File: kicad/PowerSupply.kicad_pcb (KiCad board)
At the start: 2 copper layers, 93 x 116 mm, 111 parts, among them J1 USB_A, J2 Display, J3 USART, J4 Terminal, Q1 MMBT3904, Q2 MMBT3904, Q3 MMBT3904, Q4 MMBT3904, SW1 ENC0 (Voltage), SW2 ENC1 (Current), SW4 RST, U1 OPA4196, U10 STM32F373C8Tx, U2 OPA4196, U3 LD1086D2T33, U5 FQP17P10, U6 FQP17P10, U7 FQP17P10, U8 FQP17P10, Y1 Crystal

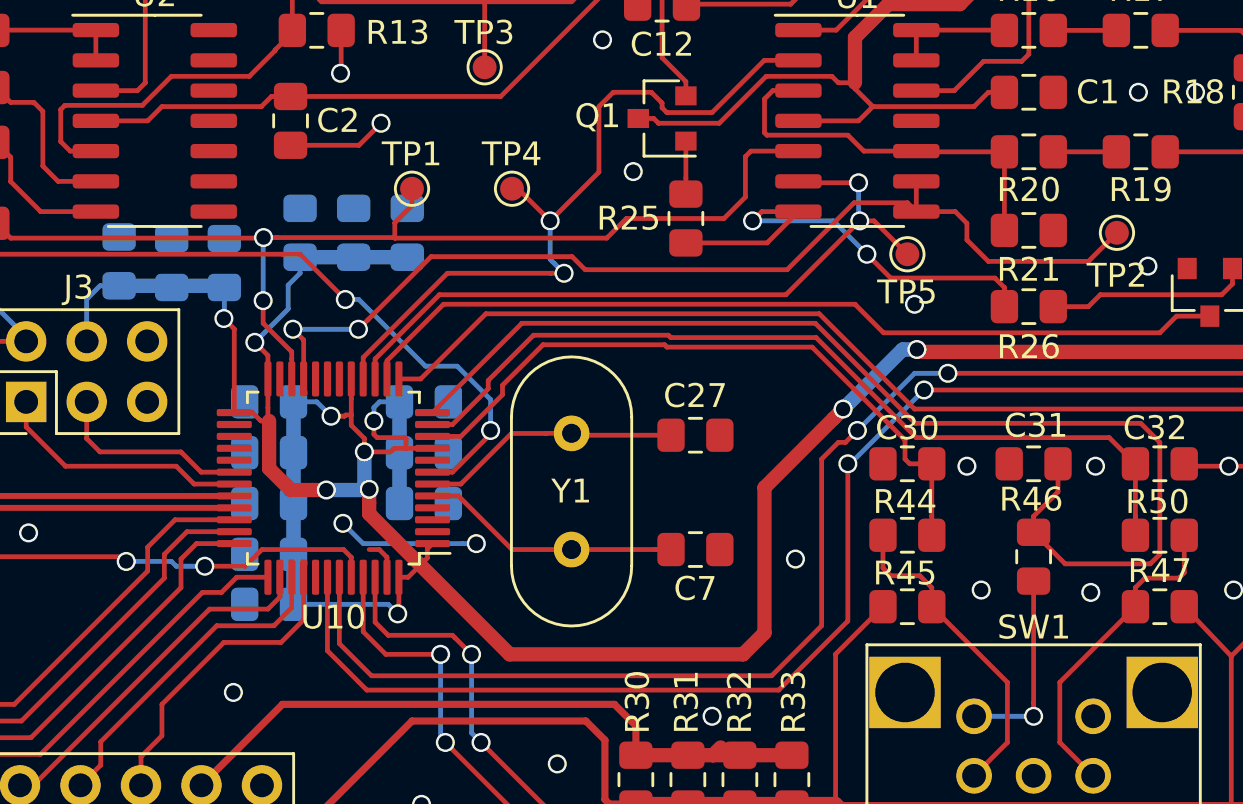
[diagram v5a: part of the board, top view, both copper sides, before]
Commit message: MCU and Crystal caps all grounded at one point
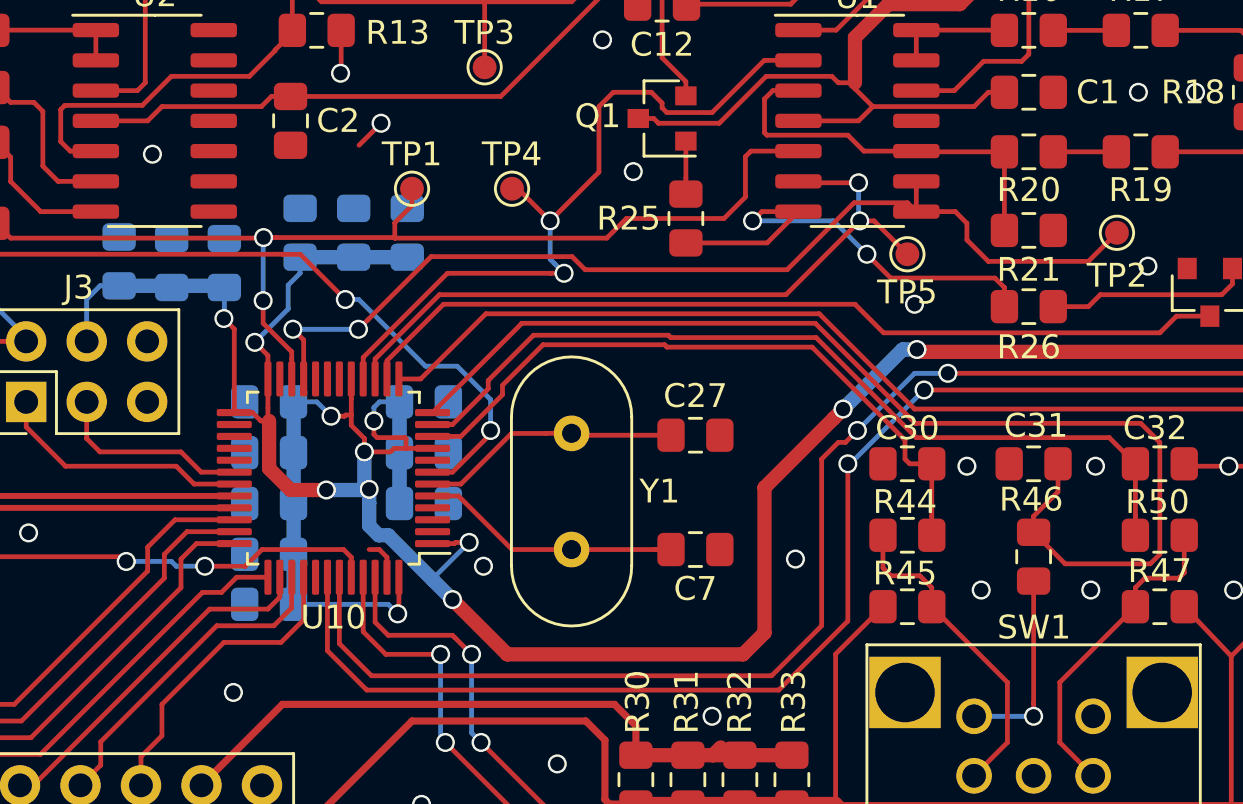
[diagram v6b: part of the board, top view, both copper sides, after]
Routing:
- net GNDREF: track 51.6 -> 42.7 mm, vias 47 -> 48
- net +3V3: track 315.5 -> 317.4 mm, vias 10 -> 12
- net (no net): vias 1 -> 0
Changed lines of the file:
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@@
     (thickness 1.6)
     (drawings 6)
-    (tracks 862)
+    (tracks 864)
     (zones 0)
     (modules 111)
@@
     (descr "Crystal THT HC-49/U http://5hertz.com/pdfs/04404_D.pdf")
     (tags "THT crystalHC-49/U")
-    (fp_text reference Y1 (at 2.44 0 180) (layer F.SilkS)
+    (fp_text reference Y1 (at 2.44 3.7 180) (layer F.SilkS)
       (effects (font (size 1 1) (thickness 0.15)))
     )
@@
   (gr_line (start 0 0) (end 93 0) (layer Edge.Cuts) (width 0.05))
   (gr_line (start 0 0) (end 0 116) (layer Edge.Cuts) (width 0.05))
-  (via (at 5.2 91.7) (size 0.8) (drill 0.6) (layers F.Cu B.Cu) (net 0))
+  (via (at 5.2 91.7) (size 0.8) (drill 0.6) (layers F.Cu B.Cu) (net 1))
   (segment (start 89.525 79.71) (end 89.54 79.725) (width 1) (layer F.Cu) (net 1))
   (segment (start 89.525 76) (end 89.525 79.71) (width 1) (layer F.Cu) (net 1))
@@
   (segment (start 6.025 107) (end 8.525 104.5) (width 0.2) (layer B.Cu) (net 1))
   (segment (start 8.25 88.25) (end 8.25 77.75) (width 0.2) (layer F.Cu) (net 1))
-  (via (at 30.4 101.9) (size 0.8) (drill 0.6) (layers F.Cu B.Cu) (net 1))
-  (segment (start 30.4 101.9) (end 31.251262 102.751262) (width 0.2) (layer B.Cu) (net 1))
-  (segment (start 31.251262 102.751262) (end 35.434325 102.751262) (width 0.2) (layer B.Cu) (net 1))
-  (segment (start 35.434325 102.751262) (end 36.00001 102.751262) (width 0.2) (layer B.Cu) (net 1))
   (via (at 13.8 87.7) (size 0.8) (drill 0.6) (layers F.Cu B.Cu) (net 1))
   (segment (start 13.775 87.725) (end 13.8 87.7) (width 0.2) (layer F.Cu) (net 1))
   (via (at 32 85.1) (size 0.8) (drill 0.6) (layers F.Cu B.Cu) (net 1))
-  (segment (start 28.2 86.025) (end 31.075 86.025) (width 0.2) (layer F.Cu) (net 1))
   (segment (start 31.075 86.025) (end 32 85.1) (width 0.2) (layer F.Cu) (net 1))
   (via (at 30.3 83) (size 0.8) (drill 0.6) (layers F.Cu B.Cu) (net 1))
@@
   (via (at 37.4 78.7) (size 0.8) (drill 0.6) (layers F.Cu B.Cu) (net 1))
   (via (at 54.4 92.7) (size 0.8) (drill 0.6) (layers F.Cu B.Cu) (net 1))
-  (via (at 36.00001 102.751262) (size 0.8) (drill 0.6) (layers F.Cu B.Cu) (net 1))
   (via (at 64.2 91.1) (size 0.8) (drill 0.6) (layers F.Cu B.Cu) (net 1))
   (via (at 87.49 98.3) (size 0.8) (drill 0.6) (layers F.Cu B.Cu) (net 1))
@@
   (via (at 84.1 18.5) (size 0.8) (drill 0.6) (layers F.Cu B.Cu) (net 1))
   (via (at 62 99.5) (size 0.8) (drill 0.6) (layers F.Cu B.Cu) (net 1))
-  (via (at 61.8 104.8) (size 0.8) (drill 0.6) (layers F.Cu B.Cu) (net 1))
+  (via (at 61.8 104.7) (size 0.8) (drill 0.6) (layers F.Cu B.Cu) (net 1))
+  (via (at 22.4 86.4) (size 0.8) (drill 0.6) (layers F.Cu B.Cu) (net 1))
+  (via (at 36.3 103.7) (size 0.8) (drill 0.6) (layers F.Cu B.Cu) (net 1))
   (segment (start 62 3.3) (end 6 3.3) (width 5) (layer F.Cu) (net 2))
   (segment (start 69.3 3.3) (end 62 3.3) (width 5) (layer F.Cu) (net 2))
@@
   (segment (start 75.275 94.7) (end 54.6 94.7) (width 0.6) (layer F.Cu) (net 3))
   (via (at 51.4 97.1) (size 0.8) (drill 0.6) (layers F.Cu B.Cu) (net 3))
-  (segment (start 33.1375 104.1625) (end 33.65 103.65) (width 0.2) (layer F.Cu) (net 3))
-  (segment (start 32.75 104.1625) (end 33.1375 104.1625) (width 0.2) (layer F.Cu) (net 3))
-  (segment (start 33.94179 103.35821) (end 33.65 103.65) (width 0.2) (layer F.Cu) (net 3))
-  (segment (start 34.1625 102.75) (end 33.94179 102.97071) (width 0.2) (layer F.Cu) (net 3))
-  (segment (start 33.94179 102.97071) (end 33.94179 103.35821) (width 0.2) (layer F.Cu) (net 3))
   (via (at 31.3 98.9) (size 0.8) (drill 0.6) (layers F.Cu B.Cu) (net 3))
   (segment (start 31.3 98.9) (end 32.4 98.9) (width 0.2) (layer F.Cu) (net 3))
@@
   (segment (start 32.55 98.75) (end 33.05 98.75) (width 0.2) (layer F.Cu) (net 3))
   (segment (start 33.05 98.75) (end 34.1625 98.75) (width 0.2) (layer F.Cu) (net 3))
-  (segment (start 33.65 103.65) (end 31.50001 101.50001) (width 0.6) (layer F.Cu) (net 3))
   (via (at 31.50001 100.469455) (size 0.8) (drill 0.6) (layers F.Cu B.Cu) (net 3))
   (segment (start 29.7 100.5) (end 31.469465 100.5) (width 0.6) (layer B.Cu) (net 3))
@@
   (segment (start 31.3 100.269445) (end 31.50001 100.469455) (width 0.6) (layer B.Cu) (net 3))
   (segment (start 31.3 98.9) (end 31.3 100.269445) (width 0.6) (layer B.Cu) (net 3))
-  (segment (start 31.50001 101.03514) (end 31.50001 100.469455) (width 0.6) (layer F.Cu) (net 3))
-  (segment (start 31.50001 101.50001) (end 31.50001 101.03514) (width 0.6) (layer F.Cu) (net 3))
   (segment (start 67.7 113.9) (end 81 113.9) (width 0.6) (layer F.Cu) (net 3))
   (segment (start 81 113.9) (end 83.6 111.3) (width 0.6) (layer F.Cu) (net 3))
@@
   (segment (start 3.975 100) (end 3.975 107) (width 0.2) (layer B.Cu) (net 3))
   (segment (start 3.975 107) (end 3.975 112.735) (width 0.2) (layer B.Cu) (net 3))
-  (segment (start 51.000001 97.499999) (end 51.4 97.1) (width 0.6) (layer F.Cu) (net 3))
-  (segment (start 48.1 100.4) (end 51.000001 97.499999) (width 0.6) (layer F.Cu) (net 3))
-  (segment (start 48.1 106.5) (end 48.1 100.4) (width 0.6) (layer F.Cu) (net 3))
-  (segment (start 47.2 107.4) (end 48.1 106.5) (width 0.6) (layer F.Cu) (net 3))
-  (segment (start 37.4 107.4) (end 47.2 107.4) (width 0.6) (layer F.Cu) (net 3))
-  (segment (start 33.65 103.65) (end 37.4 107.4) (width 0.6) (layer F.Cu) (net 3))
   (segment (start 42.7 113.685) (end 41.585 113.685) (width 0.3) (layer F.Cu) (net 3))
   (segment (start 41.585 113.685) (end 41.4 113.5) (width 0.3) (layer F.Cu) (net 3))
@@
   (segment (start 5.84 114.6) (end 4.14 112.9) (width 0.3) (layer F.Cu) (net 3))
   (segment (start 28.9 114.6) (end 5.84 114.6) (width 0.3) (layer F.Cu) (net 3))
+  (segment (start 31.50001 101.03514) (end 31.5 101.03515) (width 0.6) (layer B.Cu) (net 3))
+  (segment (start 31.50001 100.469455) (end 31.50001 101.03514) (width 0.6) (layer B.Cu) (net 3))
+  (segment (start 31.5 101.03515) (end 31.5 102) (width 0.6) (layer B.Cu) (net 3))
+  (segment (start 31.5 102) (end 31.9 102.4) (width 0.6) (layer B.Cu) (net 3))
+  (via (at 35 105.1) (size 0.8) (drill 0.6) (layers F.Cu B.Cu) (net 3))
+  (segment (start 31.9 102.4) (end 32.3 102.4) (width 0.6) (layer B.Cu) (net 3))
+  (segment (start 51.000001 97.499999) (end 51.4 97.1) (width 0.6) (layer F.Cu) (net 3))
+  (segment (start 48.1 100.4) (end 51.000001 97.499999) (width 0.6) (layer F.Cu) (net 3))
+  (segment (start 48.1 106.5) (end 48.1 100.4) (width 0.6) (layer F.Cu) (net 3))
+  (segment (start 47.2 107.4) (end 48.1 106.5) (width 0.6) (layer F.Cu) (net 3))
+  (segment (start 35 105.1) (end 37.3 107.4) (width 0.6) (layer F.Cu) (net 3))
+  (segment (start 37.3 107.4) (end 47.2 107.4) (width 0.6) (layer F.Cu) (net 3))
+  (via (at 35.7 102.7) (size 0.8) (drill 0.6) (layers F.Cu B.Cu) (net 3))
+  (segment (start 34.2 104.2) (end 35.7 102.7) (width 0.2) (layer B.Cu) (net 3))
+  (segment (start 34.2 104.3) (end 34.2 104.2) (width 0.2) (layer B.Cu) (net 3))
+  (segment (start 32.3 102.4) (end 34.2 104.3) (width 0.6) (layer B.Cu) (net 3))
+  (segment (start 34.2 104.3) (end 35 105.1) (width 0.6) (layer B.Cu) (net 3))
+  (segment (start 35.084315 102.75) (end 34.1625 102.75) (width 0.2) (layer F.Cu) (net 3))
+  (segment (start 35.7 102.7) (end 35.134315 102.7) (width 0.2) (layer F.Cu) (net 3))
+  (segment (start 35.134315 102.7) (end 35.084315 102.75) (width 0.2) (layer F.Cu) (net 3))
   (segment (start 35.25 100.75) (end 34.1625 100.75) (width 0.2) (layer F.Cu) (net 4))
   (segment (start 40 103) (end 37.5 103) (width 0.2) (layer F.Cu) (net 4))
@@
     (connect_pads (clearance 0.2))
     (min_thickness 0.2)
-    (fill yes (arc_segments 32) (thermal_gap 0.508) (thermal_bridge_width 0.508))
+    (fill (arc_segments 32) (thermal_gap 0.3) (thermal_bridge_width 0.25))
     (polygon
       (pts
@@
     (connect_pads (clearance 0.2))
     (min_thickness 0.2)
-    (fill yes (arc_segments 32) (thermal_gap 0.508) (thermal_bridge_width 0.508))
+    (fill (arc_segments 32) (thermal_gap 0.3) (thermal_bridge_width 0.25))
     (polygon
       (pts

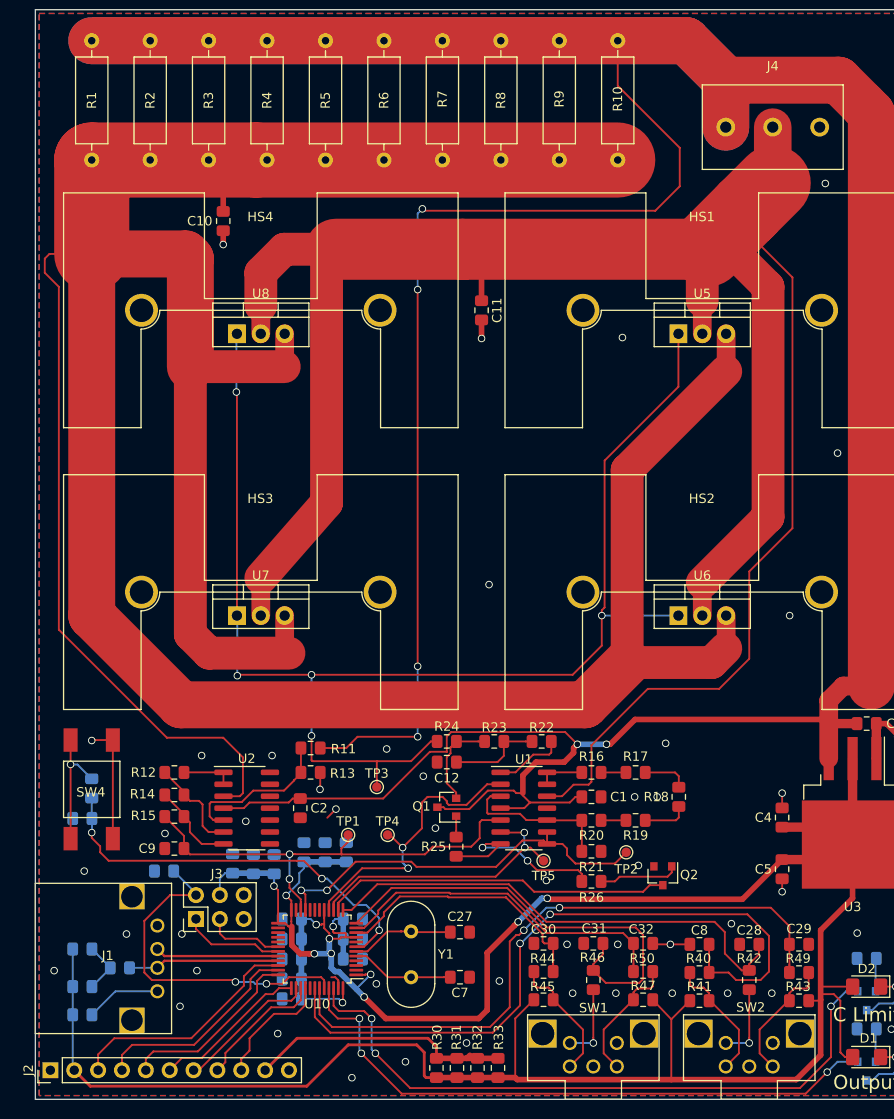
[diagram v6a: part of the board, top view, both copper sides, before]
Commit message: Fixed Silkscreen stuff
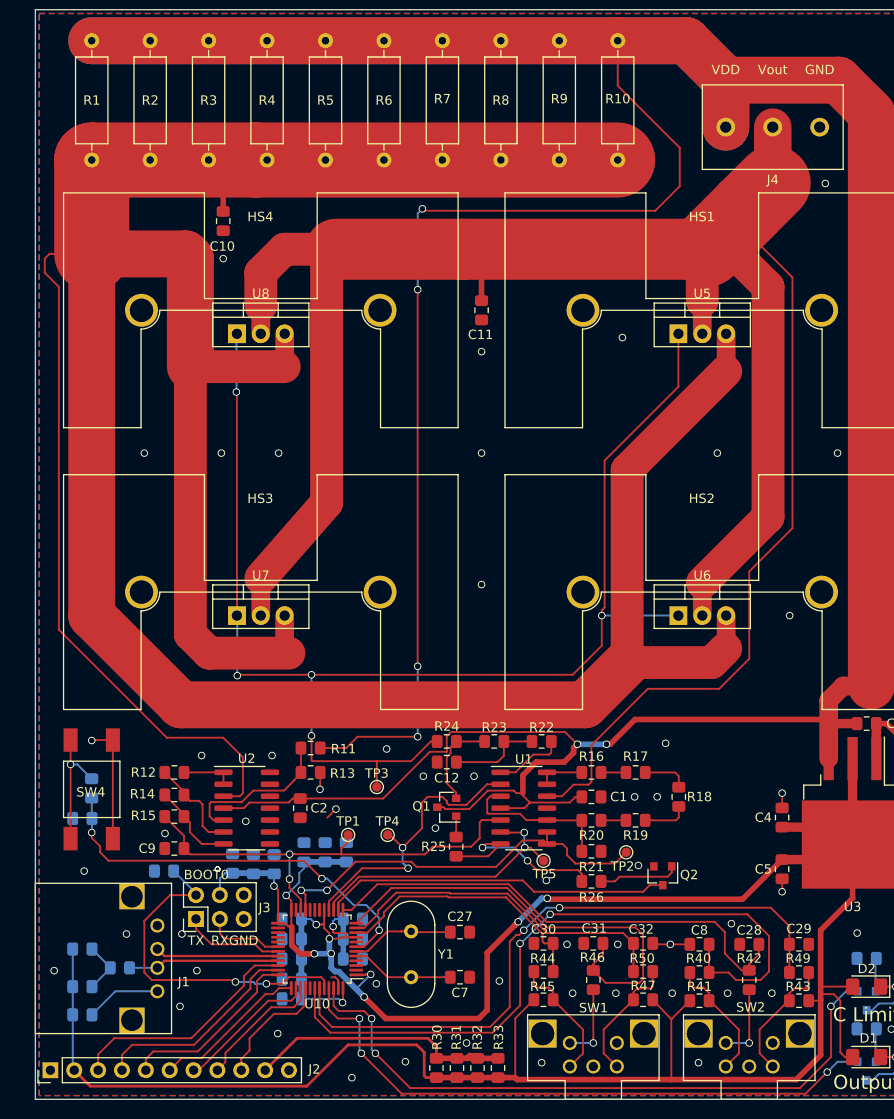
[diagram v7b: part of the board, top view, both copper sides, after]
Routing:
- net GNDREF: track 42.7 -> 39.3 mm, vias 48 -> 59
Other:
- board text added: "BOOT0"
- board text added: "GND"
- board text added: "RX"
- board text added: "TX"
- board text added: "VDD"
- board text added: "Vout"

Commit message: Minor fixes
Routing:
- net GNDREF: vias 59 -> 56
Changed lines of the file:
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@@
     (thickness 1.6)
     (drawings 13)
-    (tracks 873)
+    (tracks 870)
     (zones 0)
     (modules 111)
@@
       (plotinvisibletext false)
       (padsonsilk false)
-      (subtractmaskfromsilk false)
+      (subtractmaskfromsilk true)
       (outputformat 1)
       (mirror false)
@@
     (tags "capacitor handsolder")
     (attr smd)
-    (fp_text reference C6 (at 0 -2) (layer B.SilkS)
+    (fp_text reference C6 (at 0 -1.6) (layer B.SilkS)
       (effects (font (size 1 1) (thickness 0.15)) (justify mirror))
     )
@@
   (via (at 22.4 86.4) (size 0.8) (drill 0.6) (layers F.Cu B.Cu) (net 1))
   (via (at 36.3 103.7) (size 0.8) (drill 0.6) (layers F.Cu B.Cu) (net 1))
-  (via (at 19.4 91.5) (size 0.6) (drill 0.3) (layers F.Cu B.Cu) (net 1))
-  (via (at 19.4 91.5) (size 0.6) (drill 0.3) (layers F.Cu B.Cu) (net 1))
-  (via (at 19.4 91.5) (size 0.6) (drill 0.3) (layers F.Cu B.Cu) (net 1))
   (via (at 11.6 47.2) (size 0.8) (drill 0.6) (layers F.Cu B.Cu) (net 1))
   (via (at 25.9 47.2) (size 0.8) (drill 0.6) (layers F.Cu B.Cu) (net 1))
